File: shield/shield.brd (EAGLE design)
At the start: 102.5 x 66 mm, 13 parts, among them IC1 LM75, Q1 BUZ11BV, Q2 BUZ11BV, Q3 BUZ11BV, Q4 BUZ11BV, U1 TLC5925IDWR

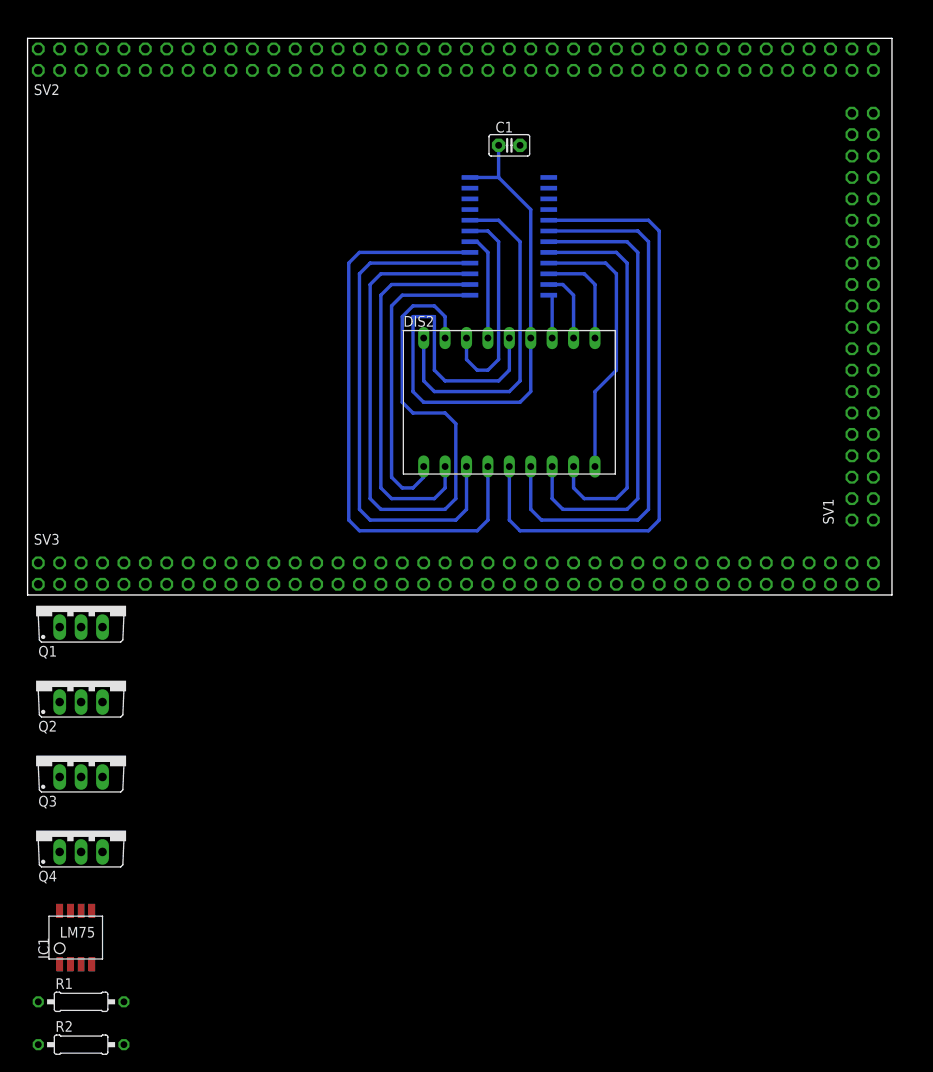
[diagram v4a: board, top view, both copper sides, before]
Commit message: Update shield schematic and pcb
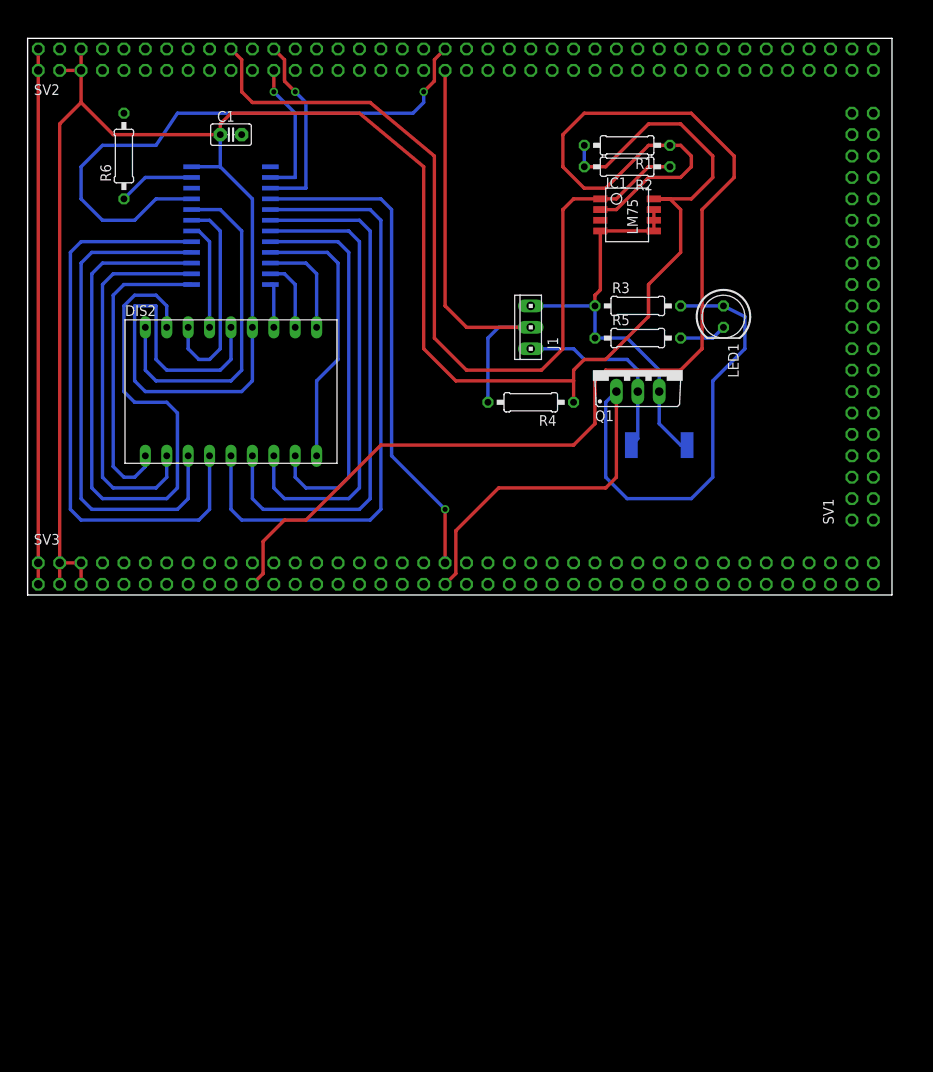
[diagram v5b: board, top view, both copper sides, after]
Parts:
- removed Q2, Q3, Q4: BUZ11BV, transistor-power:TO220BV
- added D1: 1.5SMCJ33A, seb:DO214AB
- added J1: (no value), con-amp:10X03MTA
- added LED1: (no value), led:LED5MM
- added R3, R4: 10k, rcl:0207/10
- added R5: 330, rcl:0207/10
- added R6: 330R, rcl:0207/10
- DIS2: value HD-K121 -> HDSP-521E
- Q1: value BUZ11BV -> IPP114N03L
- moved R2 122.6 mm to (69.8, 62.2), turned to 180 degrees
- moved R1 120.5 mm to (69.8, 64.8), turned to 180 degrees
- moved IC1 108.7 mm to (69.8, 57.1), turned to 270 degrees
- moved Q1 71.7 mm to (71.1, 38.1)
- moved C1 33.0 mm to (22.9, 66.0)
- moved DIS2 33.0 mm to (22.9, 35.6)
- moved U1 33.0 mm to (22.9, 55.2)
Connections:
- new net N$18: LED1.K, R5.2
- new net N$20: R6.1, U1.23
- net +3V3: now also R4.1
- net GND: now also D1.A, J1.1, Q1.S, R3.1, R5.1, R6.2
- net N$17: now also D1.K, J1.3, Q1.D; no longer Q1.S, Q2.S, Q3.S, Q4.S
- net P77: now also LED1.A, R3.2
- net P78: now also J1.2, R4.2; no longer Q2.G
- net P79: now also U1.4; no longer Q3.G
- net P80: now also U1.21; no longer Q4.G
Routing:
- net +3V3: track 80.7 -> 305.5 mm
- net P41: track 0.00 -> 154.9 mm
- net P40: track 0.00 -> 102.1 mm
- net P77: track 0.00 -> 92.8 mm
- net P80: track 0.00 -> 70.7 mm, vias 0 -> 1
- net +5V: track 0.00 -> 63.5 mm
- net P79: track 0.00 -> 59.4 mm, vias 0 -> 1
- net P78: track 0.00 -> 52.4 mm
- net GND: track 0.00 -> 49.4 mm
- net N$17: track 0.00 -> 23.0 mm
- net P48: track 0.00 -> 22.3 mm, vias 0 -> 1
- net P46: track 0.00 -> 16.7 mm, vias 0 -> 1
- net N$20: track 0.00 -> 9.08 mm
- net N$18: track 0.00 -> 5.61 mm

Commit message: Update board file
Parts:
- moved R4 29.6 mm to (53.3, 63.5)
- moved IC1 26.2 mm to (57.1, 34.3)
- moved R2 26.2 mm to (57.1, 39.4), turned to 0 degrees
- moved R1 25.0 mm to (57.1, 43.2), turned to 0 degrees
- moved R3 18.5 mm to (76.2, 63.5)
- moved R5 18.5 mm to (76.2, 59.7)
- moved LED1 18.5 mm to (86.4, 62.2)
- moved D1 18.2 mm to (81.3, 45.7), flipped to the top, turned to 0 degrees
- moved Q1 18.2 mm to (78.7, 54.6)
- moved J1 11.7 mm to (61.0, 54.6)
- moved R6 2.54 mm to (10.2, 66.0)
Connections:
- removed net +5V: SV2.1, SV2.2, SV3.1, SV3.2
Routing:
- net GND: track 49.4 -> 169.1 mm
- net P41: track 154.9 -> 54.7 mm
- net +5V: track 63.5 -> 0.00 mm
- net +3V3: track 305.5 -> 250.5 mm
- net P40: track 102.1 -> 56.5 mm
- net P78: track 52.4 -> 28.5 mm
- net N$17: track 23.0 -> 29.1 mm
- net P77: track 92.8 -> 87.6 mm
- net P48: track 22.3 -> 25.5 mm
- net P46: track 16.7 -> 18.8 mm
- net P80: track 70.7 -> 68.9 mm
- net N$20: track 9.08 -> 8.03 mm
- added copper zone on layer 1, net GND
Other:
- board text added: "Boomerang I/O Shield"

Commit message: Add capacitor
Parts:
- added C2: 100n, capacitor-wima:C2.5-2
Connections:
- net +3V3: now also C2.1
- net GND: now also C2.2
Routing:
- net +3V3: track 250.5 -> 264.5 mm
- net P77: track 87.6 -> 88.7 mm
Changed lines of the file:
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@@
 <element name="R6" library="rcl" package="0207/10" value="330R" x="10.16" y="66.04" rot="R90"/>
 <element name="D1" library="seb" package="DO214AB" value="1.5SMCJ33A" x="81.28" y="45.72"/>
+<element name="C2" library="capacitor-wima" package="C2.5-2" value="100n" x="56.84875625" y="28.424378125" rot="R180"/>
 </elements>
 <signals>
@@
 <wire x1="97.79" y1="71.12" x2="88.9" y2="71.12" width="0.4064" layer="1"/>
 <wire x1="88.9" y1="71.12" x2="88.9" y2="73.66" width="0.4064" layer="1"/>
+<contactref element="C2" pad="2"/>
 </signal>
 <signal name="P14">
@@
 <wire x1="76.2" y1="49.53" x2="76.2" y2="52.07" width="0.4064" layer="16"/>
 <wire x1="49.53" y1="19.05" x2="52.07" y2="21.59" width="0.4064" layer="1"/>
-<wire x1="52.07" y1="21.59" x2="54.61" y2="21.59" width="0.4064" layer="1"/>
-<wire x1="54.61" y1="21.59" x2="66.04" y2="33.02" width="0.4064" layer="1"/>
-<wire x1="66.04" y1="33.02" x2="66.04" y2="40.64" width="0.4064" layer="1"/>
+<wire x1="52.07" y1="21.59" x2="56.424321875" y2="21.59" width="0.4064" layer="1"/>
+<wire x1="56.424321875" y1="21.59" x2="66.04" y2="31.205678125" width="0.4064" layer="1"/>
+<wire x1="66.04" y1="31.205678125" x2="66.04" y2="40.64" width="0.4064" layer="1"/>
 <wire x1="66.04" y1="40.64" x2="69.85" y2="44.45" width="0.4064" layer="1"/>
 <wire x1="69.85" y1="44.45" x2="69.85" y2="45.72" width="0.4064" layer="1"/>
@@
 <wire x1="22.86" y1="68.58" x2="21.59" y2="67.31" width="0.4064" layer="16"/>
 <wire x1="21.59" y1="67.31" x2="21.59" y2="66.04" width="0.4064" layer="16"/>
+<contactref element="C2" pad="1"/>
+<wire x1="60.325" y1="35.56" x2="62.4133875" y2="35.56" width="0.4064" layer="1"/>
+<wire x1="62.4133875" y1="35.56" x2="63.50126875" y2="34.47211875" width="0.4064" layer="1"/>
+<wire x1="63.50126875" y1="34.47211875" x2="63.50126875" y2="30.2387" width="0.4064" layer="1"/>
+<wire x1="63.50126875" y1="30.2387" x2="61.686946875" y2="28.424378125" width="0.4064" layer="1"/>
+<wire x1="61.686946875" y1="28.424378125" x2="58.11875625" y2="28.424378125" width="0.4064" layer="1"/>
 </signal>
 <signal name="N$1">
@@
 </signal>
 </signals>
-<errors>
-</errors>
 </board>
 </drawing>

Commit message: update shield
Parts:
- moved C2 3.87 mm to (53.8, 30.8)
- moved IC1 3.87 mm to (54.1, 36.7)
- moved R1 3.87 mm to (54.1, 45.6)
- moved R2 3.87 mm to (54.1, 41.8)
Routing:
- net P40: track 56.5 -> 52.7 mm
- net P41: track 54.7 -> 53.6 mm
- net +3V3: track 264.5 -> 265.1 mm
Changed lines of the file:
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@@
 <element name="C1" library="capacitor-wima" package="C2.5-2" value="100n" x="22.86" y="66.04"/>
 <element name="Q1" library="transistor-power" package="TO220BV" value="IPP114N03L" x="78.74" y="54.61"/>
-<element name="IC1" library="lm75" package="SO8_LM75" value="LM75" x="57.15" y="34.29" rot="R270"/>
-<element name="R1" library="rcl" package="0207/10" value="10k" x="57.15" y="43.18"/>
-<element name="R2" library="rcl" package="0207/10" value="10k" x="57.15" y="39.37"/>
+<element name="IC1" library="lm75" package="SO8_LM75" value="LM75" x="54.12613125" y="36.709096875" rot="R270"/>
+<element name="R1" library="rcl" package="0207/10" value="10k" x="54.12613125" y="45.599096875"/>
+<element name="R2" library="rcl" package="0207/10" value="10k" x="54.12613125" y="41.789096875"/>
 <element name="J1" library="con-amp" package="10X03MTA" value="" x="60.96" y="54.61" rot="R90"/>
 <element name="R3" library="rcl" package="0207/10" value="10k" x="76.2" y="63.5"/>
@@
 <element name="R6" library="rcl" package="0207/10" value="330R" x="10.16" y="66.04" rot="R90"/>
 <element name="D1" library="seb" package="DO214AB" value="1.5SMCJ33A" x="81.28" y="45.72"/>
-<element name="C2" library="capacitor-wima" package="C2.5-2" value="100n" x="56.84875625" y="28.424378125" rot="R180"/>
+<element name="C2" library="capacitor-wima" package="C2.5-2" value="100n" x="53.8248875" y="30.843475" rot="R180"/>
 </elements>
 <signals>
@@
 <wire x1="71.12" y1="59.69" x2="71.12" y2="63.5" width="0.4064" layer="16"/>
 <contactref element="R6" pad="2"/>
-<wire x1="53.975" y1="31.75" x2="60.325" y2="31.75" width="0.4064" layer="1"/>
-<wire x1="60.325" y1="31.75" x2="60.325" y2="33.02" width="0.4064" layer="1"/>
-<wire x1="60.325" y1="33.02" x2="60.325" y2="34.29" width="0.4064" layer="1"/>
+<wire x1="50.95113125" y1="34.169096875" x2="57.30113125" y2="34.169096875" width="0.4064" layer="1"/>
+<wire x1="57.30113125" y1="34.169096875" x2="57.30113125" y2="35.439096875" width="0.4064" layer="1"/>
+<wire x1="57.30113125" y1="35.439096875" x2="57.30113125" y2="36.709096875" width="0.4064" layer="1"/>
 <contactref element="D1" pad="A"/>
 <wire x1="17.78" y1="76.2" x2="15.24" y2="73.66" width="0.4064" layer="1"/>
@@
 <contactref element="IC1" pad="1"/>
 <contactref element="R2" pad="1"/>
-<wire x1="53.975" y1="35.56" x2="53.34" y2="35.56" width="0.4064" layer="1"/>
-<wire x1="53.34" y1="35.56" x2="52.07" y2="36.83" width="0.4064" layer="1"/>
-<wire x1="52.07" y1="36.83" x2="52.07" y2="39.37" width="0.4064" layer="1"/>
-<wire x1="52.07" y1="39.37" x2="48.26" y2="39.37" width="0.4064" layer="1"/>
-<wire x1="48.26" y1="39.37" x2="38.1" y2="48.26" width="0.4064" layer="1"/>
+<wire x1="50.95113125" y1="37.979096875" x2="50.31613125" y2="37.979096875" width="0.4064" layer="1"/>
+<wire x1="50.31613125" y1="37.979096875" x2="49.04613125" y2="39.249096875" width="0.4064" layer="1"/>
+<wire x1="49.04613125" y1="39.249096875" x2="49.04613125" y2="41.789096875" width="0.4064" layer="1"/>
+<wire x1="49.04613125" y1="41.789096875" x2="45.23613125" y2="41.789096875" width="0.4064" layer="1"/>
+<wire x1="45.23613125" y1="41.789096875" x2="38.1" y2="48.26" width="0.4064" layer="1"/>
 <wire x1="38.1" y1="48.26" x2="38.1" y2="57.15" width="0.4064" layer="1"/>
 <wire x1="38.1" y1="57.15" x2="24.13" y2="71.12" width="0.4064" layer="1"/>
@@
 <contactref element="IC1" pad="2"/>
 <contactref element="R1" pad="1"/>
-<wire x1="52.07" y1="43.18" x2="54.61" y2="43.18" width="0.4064" layer="1"/>
-<wire x1="54.61" y1="43.18" x2="57.15" y2="40.64" width="0.4064" layer="1"/>
-<wire x1="57.15" y1="40.64" x2="57.15" y2="35.56" width="0.4064" layer="1"/>
-<wire x1="57.15" y1="35.56" x2="55.88" y2="34.29" width="0.4064" layer="1"/>
-<wire x1="55.88" y1="34.29" x2="53.975" y2="34.29" width="0.4064" layer="1"/>
-<wire x1="53.975" y1="34.29" x2="48.26" y2="34.29" width="0.4064" layer="1"/>
-<wire x1="48.26" y1="34.29" x2="34.29" y2="20.32" width="0.4064" layer="1"/>
+<wire x1="49.04613125" y1="45.599096875" x2="51.58613125" y2="45.599096875" width="0.4064" layer="1"/>
+<wire x1="51.58613125" y1="45.599096875" x2="54.12613125" y2="43.059096875" width="0.4064" layer="1"/>
+<wire x1="54.12613125" y1="43.059096875" x2="54.12613125" y2="37.979096875" width="0.4064" layer="1"/>
+<wire x1="54.12613125" y1="37.979096875" x2="52.85613125" y2="36.709096875" width="0.4064" layer="1"/>
+<wire x1="52.85613125" y1="36.709096875" x2="50.95113125" y2="36.709096875" width="0.4064" layer="1"/>
+<wire x1="50.95113125" y1="36.709096875" x2="47.655228125" y2="36.709096875" width="0.4064" layer="1"/>
+<wire x1="47.655228125" y1="36.709096875" x2="34.29" y2="20.32" width="0.4064" layer="1"/>
 <wire x1="34.29" y1="20.32" x2="29.21" y2="20.32" width="0.4064" layer="1"/>
 <wire x1="29.21" y1="20.32" x2="26.67" y2="17.78" width="0.4064" layer="1"/>
@@
 <wire x1="2.54" y1="15.24" x2="2.54" y2="67.31" width="0.4064" layer="1"/>
 <wire x1="2.54" y1="67.31" x2="5.08" y2="69.85" width="0.4064" layer="1"/>
-<wire x1="62.23" y1="43.18" x2="62.23" y2="39.37" width="0.4064" layer="1"/>
-<wire x1="62.23" y1="39.37" x2="62.23" y2="36.83" width="0.4064" layer="1"/>
-<wire x1="62.23" y1="36.83" x2="60.96" y2="35.56" width="0.4064" layer="1"/>
-<wire x1="60.96" y1="35.56" x2="60.325" y2="35.56" width="0.4064" layer="1"/>
+<wire x1="59.20613125" y1="45.599096875" x2="59.20613125" y2="41.789096875" width="0.4064" layer="1"/>
+<wire x1="59.20613125" y1="41.789096875" x2="59.20613125" y2="39.249096875" width="0.4064" layer="1"/>
+<wire x1="59.20613125" y1="39.249096875" x2="57.93613125" y2="37.979096875" width="0.4064" layer="1"/>
+<wire x1="57.93613125" y1="37.979096875" x2="57.30113125" y2="37.979096875" width="0.4064" layer="1"/>
 <wire x1="58.42" y1="63.5" x2="62.23" y2="63.5" width="0.4064" layer="1"/>
 <wire x1="62.23" y1="63.5" x2="66.04" y2="59.69" width="0.4064" layer="1"/>
-<wire x1="66.04" y1="59.69" x2="66.04" y2="44.45" width="0.4064" layer="1"/>
-<wire x1="66.04" y1="44.45" x2="64.77" y2="43.18" width="0.4064" layer="1"/>
-<wire x1="64.77" y1="43.18" x2="62.23" y2="43.18" width="0.4064" layer="1"/>
+<wire x1="66.04" y1="59.69" x2="66.04" y2="46.869096875" width="0.4064" layer="1"/>
+<wire x1="66.04" y1="46.869096875" x2="64.77" y2="45.599096875" width="0.4064" layer="1"/>
+<wire x1="64.77" y1="45.599096875" x2="59.20613125" y2="45.599096875" width="0.4064" layer="1"/>
 <wire x1="58.42" y1="63.5" x2="58.42" y2="66.04" width="0.4064" layer="16"/>
 <wire x1="58.42" y1="66.04" x2="54.61" y2="68.58" width="0.4064" layer="16"/>
@@
 <wire x1="21.59" y1="67.31" x2="21.59" y2="66.04" width="0.4064" layer="16"/>
 <contactref element="C2" pad="1"/>
-<wire x1="60.325" y1="35.56" x2="62.4133875" y2="35.56" width="0.4064" layer="1"/>
-<wire x1="62.4133875" y1="35.56" x2="63.50126875" y2="34.47211875" width="0.4064" layer="1"/>
-<wire x1="63.50126875" y1="34.47211875" x2="63.50126875" y2="30.2387" width="0.4064" layer="1"/>
-<wire x1="63.50126875" y1="30.2387" x2="61.686946875" y2="28.424378125" width="0.4064" layer="1"/>
-<wire x1="61.686946875" y1="28.424378125" x2="58.11875625" y2="28.424378125" width="0.4064" layer="1"/>
+<wire x1="57.30113125" y1="37.979096875" x2="59.38951875" y2="37.979096875" width="0.4064" layer="1"/>
+<wire x1="59.38951875" y1="37.979096875" x2="60.4774" y2="36.891215625" width="0.4064" layer="1"/>
+<wire x1="60.4774" y1="36.891215625" x2="60.4774" y2="32.657796875" width="0.4064" layer="1"/>
+<wire x1="60.4774" y1="32.657796875" x2="58.663078125" y2="30.843475" width="0.4064" layer="1"/>
+<wire x1="58.663078125" y1="30.843475" x2="55.0948875" y2="30.843475" width="0.4064" layer="1"/>
 </signal>
 <signal name="N$1">
